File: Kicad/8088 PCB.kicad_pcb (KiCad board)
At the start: 4 copper layers, 177.8 x 106.7 mm, 76 parts, among them J1 Bus_ISA_8bit, J2 Mini-DIN-6, J3 SPK, SW1 RESET, U1 8088, U10 8237, U11 74LS573, U12 74LS139, U13 AS6C4008, U14 AS6C1008, U15 27C512, U16 74LS138, U17 8284, U18 74LS74, U19 W83C42P, U2 74LS573, U20 74LS07, U21 74LS04, U22 8284, U23 74LS245, U24 74LS573, U25 74LS126, U26 74LS125, U3 74LS573, U4 74LS245, U5 8254, U6 8259, U7 74LS670, U8 74LS257, U9 27C512, Y1 14.31818, Y2 CRYSTAL

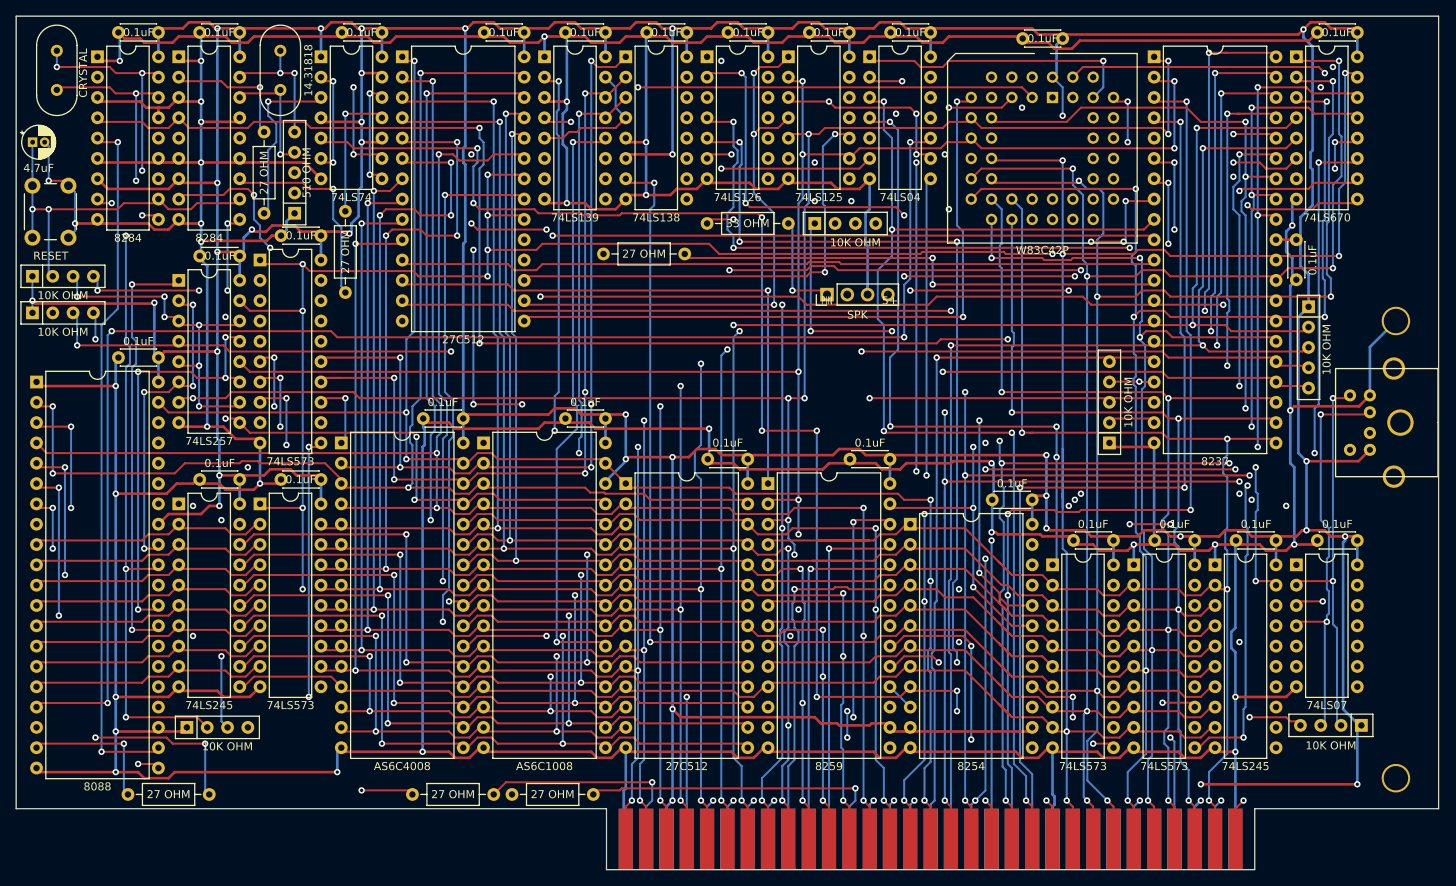
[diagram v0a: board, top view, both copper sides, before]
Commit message: Added CH376 conn
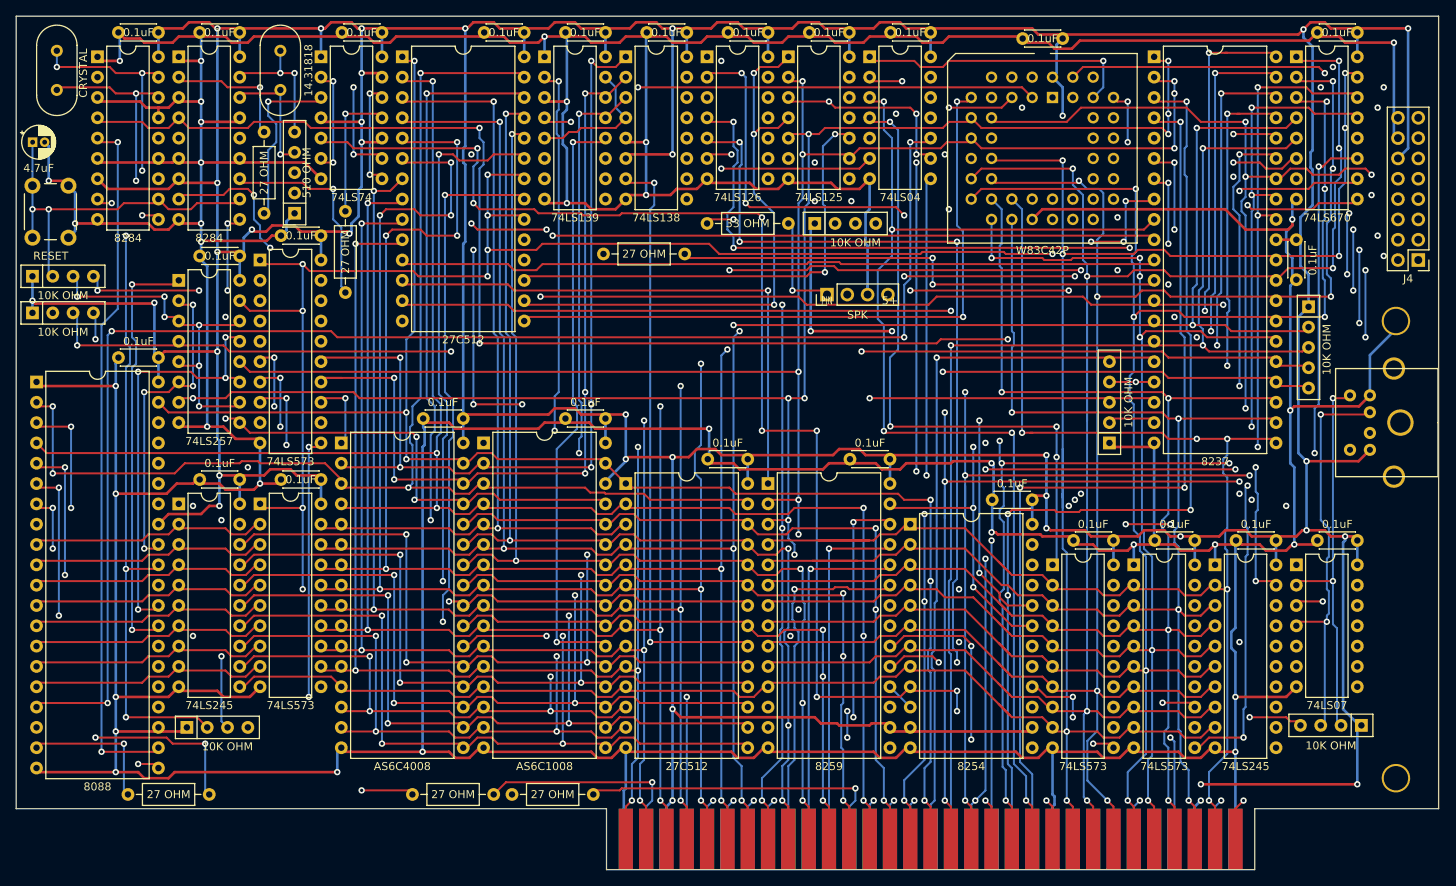
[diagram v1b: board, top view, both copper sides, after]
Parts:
- added J4: CS_7, Connector_PinHeader_2.54mm:PinHeader_2x08_P2.54mm_Vertical, F.Cu at (233.7, 68.6)
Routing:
- net /E0_CS: track 0.00 -> 119.4 mm, vias 0 -> 2
- net /D6: track 299.3 -> 353.3 mm, vias 8 -> 11
- net /D5: track 301.1 -> 355.0 mm, vias 8 -> 11
- net /IOWR: track 282.5 -> 333.5 mm, vias 9 -> 12
- net /D7: track 305.4 -> 355.3 mm, vias 8 -> 12
- net /IORD: track 290.9 -> 337.6 mm, vias 12 -> 15
- net /D4: track 301.2 -> 344.4 mm, vias 9 -> 12
- net /GND: track 1128.8 -> 1152.7 mm, vias 34 -> 35
- net /5+: track 962.9 -> 986.2 mm, vias 37 -> 38
- net /A2: track 305.0 -> 324.4 mm, vias 8 -> 10
- net /D3: track 347.9 -> 360.1 mm, vias 10 -> 11
- net /D2: track 329.0 -> 340.2 mm, vias 10 -> 11
- net /D1: track 337.9 -> 348.3 mm, vias 10 -> 11
- net /D0: track 297.0 -> 306.7 mm, vias 6 -> 7
- net /760_WR: track 68.2 -> 66.2 mm, vias 2 -> 0
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
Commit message: update for production
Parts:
- added R10: 10K OHM, Resistor_THT:R_Array_SIP5, F.Cu at (126.7, 78.7)
- added R8: 10K OHM, Resistor_THT:R_Array_SIP5, F.Cu at (131.8, 80.5)
- J4: value CS_7 -> CS7
- R12: footprint Resistor_THT:R_Array_SIP4 -> Resistor_THT:R_Array_SIP7
- moved R11 1.27 mm to (131.8, 66.5)
- moved R12 0.25 mm to (158.0, 64.0)
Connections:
- R12 pad 4: /CH_CK_ -> /EOP
- R14 pad 4: Net-(R14-Pad4) -> /NMI
- U21 pad 12: (no net) -> /IOM_
- U21 pad 13: (no net) -> /IOM
- U9 pad 22: /HOLDA -> /IOM_
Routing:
- net /IOM: track 53.2 -> 178.5 mm, vias 2 -> 6
- net /IOM_: track 0.00 -> 61.1 mm, vias 0 -> 2
- net /5+: track 986.2 -> 1032.8 mm, vias 38 -> 40
- net /GND: track 1152.7 -> 1174.4 mm
- net /NMI: track 182.6 -> 204.1 mm, vias 4 -> 6
- net /EOP: track 51.9 -> 63.3 mm, vias 1 -> 2
- net /HOLDA: track 221.9 -> 211.8 mm, vias 11 -> 10
- net /760_WR: track 66.2 -> 73.8 mm, vias 0 -> 1
- net /60_CS: track 84.3 -> 87.6 mm
- net /CH_CK: track 170.5 -> 173.2 mm, vias 9 -> 7
- net /AEN: track 145.9 -> 148.4 mm
- net /RDY1: track 208.6 -> 210.5 mm
- net /E0_CS: track 119.4 -> 121.3 mm, vias 2 -> 3
- net /80_CS: track 58.0 -> 59.7 mm
- net /CS_61_WR_: track 116.7 -> 118.4 mm
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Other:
- board text added: "BIOS ROM"
- board text added: "EMM COMPUTERS 8088 PC COMPATIBLE Copyright (C) 2024 EMM www.homebrew8088.com"
- board text added: "IO DECODING"

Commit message: 17 May 24 build
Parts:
- added R15: 10K OHM, Resistor_THT:R_Axial_DIN0207_L6.3mm_D2.5mm_P10.16mm_Horizontal, F.Cu at (94.0, 131.1)
- R12: footprint Resistor_THT:R_Array_SIP7 -> Resistor_THT:R_Array_SIP6
- R17: footprint Resistor_THT:R_Array_SIP5 -> Resistor_THT:R_Array_SIP6
- moved Y1 0.33 mm to (91.4, 47.0)
- moved R18 0.25 mm to (93.2, 62.5)
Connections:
- J2 pad : (no net) -> /GND
- R pad 1: (no net) -> /GND
- R12 pad 6: /AEN -> /760_WR
- R14 pad 3: /DEN -> /NMI
- R14 pad 4: /NMI -> Net-(R14-Pad4)
- U10 pad 5: Net-(U10-Pad5) -> /5+
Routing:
- net /5+: track 1032.8 -> 1083.7 mm, vias 40 -> 43
- net /GND: track 1174.4 -> 1195.0 mm, vias 35 -> 36
- net /AEN: track 148.4 -> 141.7 mm, vias 5 -> 9
- net /DEN: track 37.1 -> 41.2 mm
- net /NMI: track 204.1 -> 201.6 mm
- net /DACK3: track 144.9 -> 147.2 mm
- net /80_CS: track 59.7 -> 58.5 mm
- net /760_WR: track 73.8 -> 73.1 mm
- net /RESET: track 159.9 -> 159.2 mm
